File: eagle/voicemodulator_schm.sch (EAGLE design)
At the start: 38 parts, among them T1 2N5089, T2 2N5089, T3 2N5089, T4 2N5089

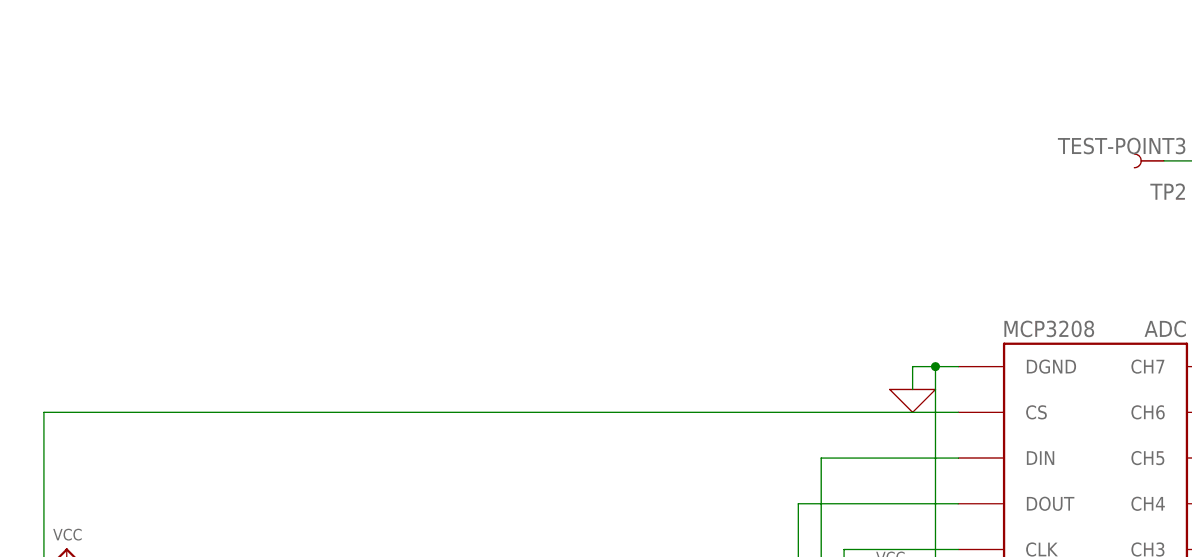
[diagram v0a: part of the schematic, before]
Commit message: USB 3.0 Type A Port Added, pinout TBD
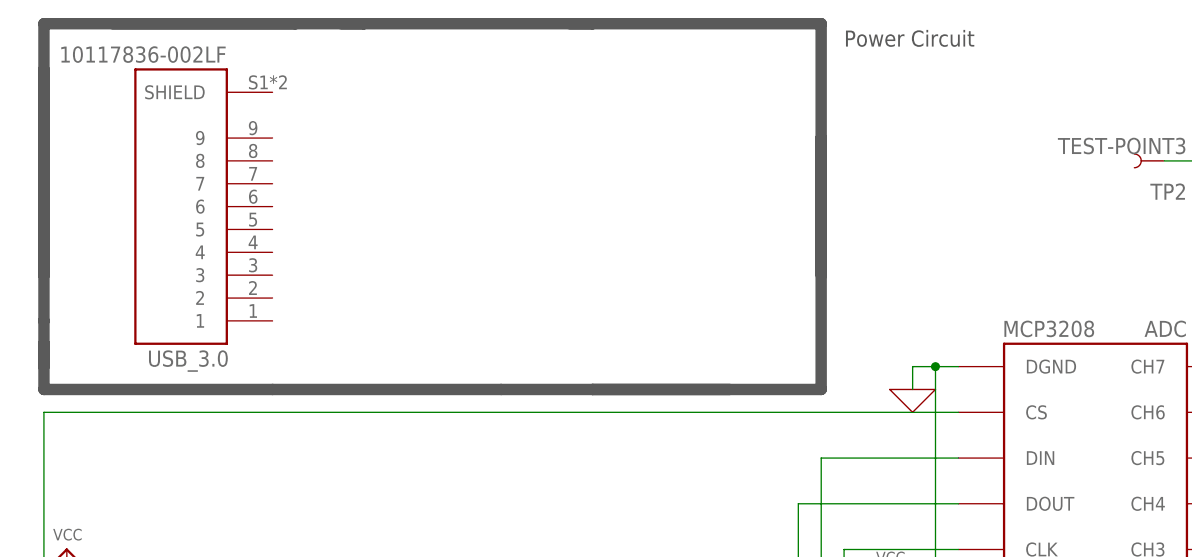
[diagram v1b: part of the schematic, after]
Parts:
- added USB_3.0: 10117836-002LF, USB_SMT_3:10117836-002LF
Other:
- note added: "Power Circuit"
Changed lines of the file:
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@@
 <part name="R18" library="resistor-shunt" library_urn="urn:adsk.eagle:library:346" deviceset="SMR-WAV" device="" package3d_urn="urn:adsk.eagle:package:25223/1"/>
 <part name="R19" library="resistor-shunt" library_urn="urn:adsk.eagle:library:346" deviceset="SMR-WAV" device="" package3d_urn="urn:adsk.eagle:package:25223/1"/>
+<part name="USB_3.0" library="USB_SMT_3" deviceset="10117836-002LF" device=""/>
 </parts>
 <sheets>
@@
 <wire x1="60.96" y1="-5.08" x2="60.96" y2="-33.02" width="1.27" layer="97"/>
 <text x="15.24" y="-2.54" size="1.778" layer="97">ISP Programming</text>
+<wire x1="-48.26" y1="83.82" x2="-48.26" y2="88.9" width="1.27" layer="97"/>
+<wire x1="-48.26" y1="88.9" x2="-48.26" y2="111.76" width="1.27" layer="97"/>
+<wire x1="-48.26" y1="88.9" x2="-48.26" y2="116.84" width="1.27" layer="97"/>
+<wire x1="38.1" y1="88.9" x2="38.1" y2="104.14" width="1.27" layer="97"/>
+<wire x1="38.1" y1="104.14" x2="38.1" y2="116.84" width="1.27" layer="97"/>
+<wire x1="38.1" y1="116.84" x2="12.7" y2="116.84" width="1.27" layer="97"/>
+<wire x1="12.7" y1="116.84" x2="10.16" y2="116.84" width="1.27" layer="97"/>
+<wire x1="12.7" y1="116.84" x2="-12.7" y2="116.84" width="1.27" layer="97"/>
+<wire x1="-12.7" y1="116.84" x2="-15.24" y2="116.84" width="1.27" layer="97"/>
+<wire x1="-12.7" y1="116.84" x2="-20.32" y2="116.84" width="1.27" layer="97"/>
+<wire x1="-20.32" y1="116.84" x2="-40.64" y2="116.84" width="1.27" layer="97"/>
+<wire x1="-20.32" y1="116.84" x2="-48.26" y2="116.84" width="1.27" layer="97"/>
+<wire x1="-48.26" y1="78.74" x2="-48.26" y2="81.28" width="1.27" layer="97"/>
+<wire x1="-48.26" y1="81.28" x2="-48.26" y2="83.82" width="1.27" layer="97"/>
+<wire x1="-22.86" y1="76.2" x2="-48.26" y2="76.2" width="1.27" layer="97"/>
+<wire x1="-48.26" y1="76.2" x2="-48.26" y2="81.28" width="1.27" layer="97"/>
+<wire x1="2.54" y1="76.2" x2="-22.86" y2="76.2" width="1.27" layer="97"/>
+<wire x1="27.94" y1="76.2" x2="12.7" y2="76.2" width="1.27" layer="97"/>
+<wire x1="12.7" y1="76.2" x2="2.54" y2="76.2" width="1.27" layer="97"/>
+<wire x1="38.1" y1="76.2" x2="12.7" y2="76.2" width="1.27" layer="97"/>
+<wire x1="38.1" y1="76.2" x2="38.1" y2="104.14" width="1.27" layer="97"/>
+<text x="40.64" y="114.3" size="1.778" layer="97">Power Circuit </text>
 </plain>
 <instances>
@@
 <attribute name="VALUE" x="130.81" y="48.641" size="1.778" layer="96" rot="R180"/>
 </instance>
+<instance part="USB_3.0" gate="G$1" x="-33.02" y="96.52" rot="R180">
+<attribute name="NAME" x="-27.686" y="80.518" size="1.778" layer="95" rot="R180"/>
+<attribute name="VALUE" x="-27.94" y="114.3" size="1.778" layer="96" rot="R180"/>
+</instance>
 </instances>

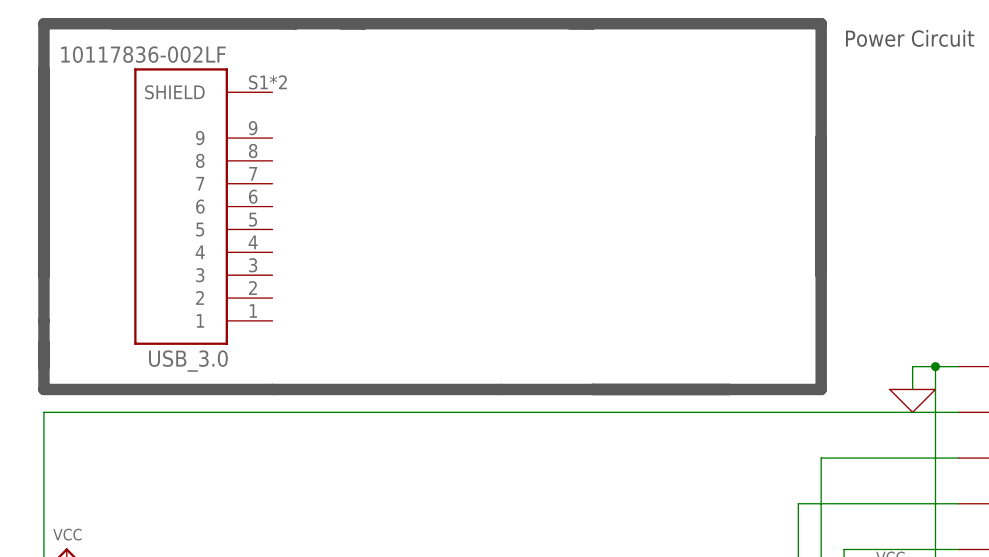
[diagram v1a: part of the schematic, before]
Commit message: Made USB 3.0 connections
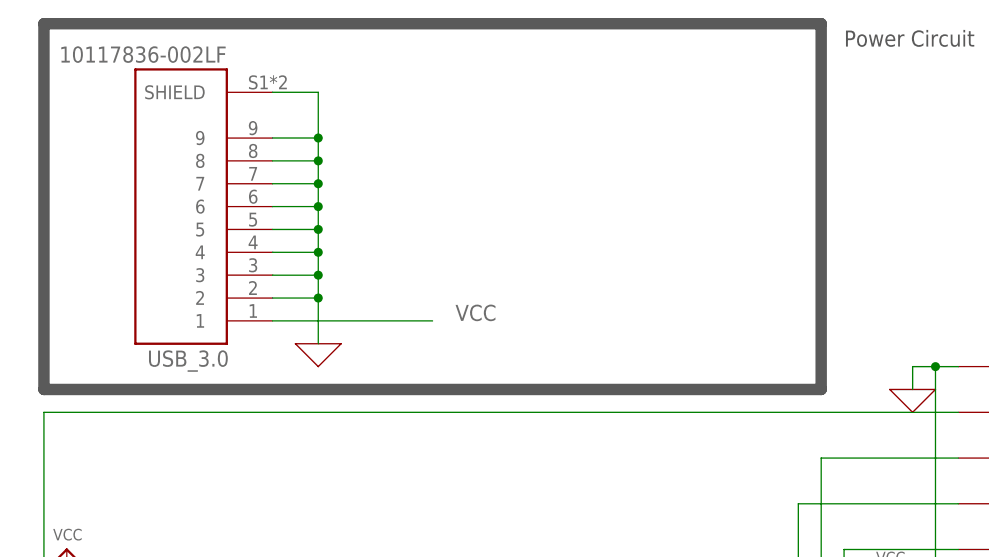
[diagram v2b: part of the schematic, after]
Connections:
- net 0: now also USB_3.0.2, USB_3.0.3, USB_3.0.4, USB_3.0.5, USB_3.0.6, USB_3.0.7, USB_3.0.8, USB_3.0.9, USB_3.0.SHIELD
- net VCC: now also USB_3.0.1
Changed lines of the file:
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@@
 <part name="R19" library="resistor-shunt" library_urn="urn:adsk.eagle:library:346" deviceset="SMR-WAV" device="" package3d_urn="urn:adsk.eagle:package:25223/1"/>
 <part name="USB_3.0" library="USB_SMT_3" deviceset="10117836-002LF" device=""/>
+<part name="X_11" library="ngspice-simulation" library_urn="urn:adsk.eagle:library:527439" deviceset="GND" device=""/>
 </parts>
 <sheets>
@@
 <wire x1="60.96" y1="-5.08" x2="60.96" y2="-33.02" width="1.27" layer="97"/>
 <text x="15.24" y="-2.54" size="1.778" layer="97">ISP Programming</text>
-<wire x1="-48.26" y1="83.82" x2="-48.26" y2="88.9" width="1.27" layer="97"/>
-<wire x1="-48.26" y1="88.9" x2="-48.26" y2="111.76" width="1.27" layer="97"/>
-<wire x1="-48.26" y1="88.9" x2="-48.26" y2="116.84" width="1.27" layer="97"/>
-<wire x1="38.1" y1="88.9" x2="38.1" y2="104.14" width="1.27" layer="97"/>
-<wire x1="38.1" y1="104.14" x2="38.1" y2="116.84" width="1.27" layer="97"/>
-<wire x1="38.1" y1="116.84" x2="12.7" y2="116.84" width="1.27" layer="97"/>
-<wire x1="12.7" y1="116.84" x2="10.16" y2="116.84" width="1.27" layer="97"/>
-<wire x1="12.7" y1="116.84" x2="-12.7" y2="116.84" width="1.27" layer="97"/>
-<wire x1="-12.7" y1="116.84" x2="-15.24" y2="116.84" width="1.27" layer="97"/>
-<wire x1="-12.7" y1="116.84" x2="-20.32" y2="116.84" width="1.27" layer="97"/>
-<wire x1="-20.32" y1="116.84" x2="-40.64" y2="116.84" width="1.27" layer="97"/>
-<wire x1="-20.32" y1="116.84" x2="-48.26" y2="116.84" width="1.27" layer="97"/>
-<wire x1="-48.26" y1="78.74" x2="-48.26" y2="81.28" width="1.27" layer="97"/>
-<wire x1="-48.26" y1="81.28" x2="-48.26" y2="83.82" width="1.27" layer="97"/>
-<wire x1="-22.86" y1="76.2" x2="-48.26" y2="76.2" width="1.27" layer="97"/>
-<wire x1="-48.26" y1="76.2" x2="-48.26" y2="81.28" width="1.27" layer="97"/>
-<wire x1="2.54" y1="76.2" x2="-22.86" y2="76.2" width="1.27" layer="97"/>
-<wire x1="27.94" y1="76.2" x2="12.7" y2="76.2" width="1.27" layer="97"/>
-<wire x1="12.7" y1="76.2" x2="2.54" y2="76.2" width="1.27" layer="97"/>
-<wire x1="38.1" y1="76.2" x2="12.7" y2="76.2" width="1.27" layer="97"/>
-<wire x1="38.1" y1="76.2" x2="38.1" y2="104.14" width="1.27" layer="97"/>
+<wire x1="-48.26" y1="76.2" x2="-48.26" y2="116.84" width="1.27" layer="97"/>
+<wire x1="38.1" y1="76.2" x2="38.1" y2="116.84" width="1.27" layer="97"/>
+<wire x1="38.1" y1="116.84" x2="-48.26" y2="116.84" width="1.27" layer="97"/>
+<wire x1="38.1" y1="76.2" x2="-48.26" y2="76.2" width="1.27" layer="97"/>
 <text x="40.64" y="114.3" size="1.778" layer="97">Power Circuit </text>
 </plain>
@@
 <attribute name="VALUE" x="-27.94" y="114.3" size="1.778" layer="96" rot="R180"/>
 </instance>
+<instance part="X_11" gate="G$1" x="-17.78" y="81.28"/>
 </instances>
 <busses>
@@
 <pinref part="X_3" gate="G$1" pin="0"/>
 <wire x1="167.64" y1="2.54" x2="167.64" y2="-7.62" width="0.1524" layer="91"/>
+</segment>
+<segment>
+<pinref part="USB_3.0" gate="G$1" pin="2"/>
+<pinref part="X_11" gate="G$1" pin="0"/>
+<wire x1="-22.86" y1="86.36" x2="-17.78" y2="86.36" width="0.1524" layer="91"/>
+<pinref part="USB_3.0" gate="G$1" pin="3"/>
+<wire x1="-17.78" y1="81.28" x2="-17.78" y2="86.36" width="0.1524" layer="91"/>
+<wire x1="-17.78" y1="86.36" x2="-17.78" y2="88.9" width="0.1524" layer="91"/>
+<wire x1="-17.78" y1="88.9" x2="-22.86" y2="88.9" width="0.1524" layer="91"/>
+<pinref part="USB_3.0" gate="G$1" pin="4"/>
+<wire x1="-22.86" y1="91.44" x2="-17.78" y2="91.44" width="0.1524" layer="91"/>
+<wire x1="-17.78" y1="91.44" x2="-17.78" y2="88.9" width="0.1524" layer="91"/>
+<junction x="-17.78" y="88.9"/>
+<junction x="-17.78" y="86.36"/>
+<pinref part="USB_3.0" gate="G$1" pin="7"/>
+<wire x1="-17.78" y1="91.44" x2="-17.78" y2="93.98" width="0.1524" layer="91"/>
+<wire x1="-17.78" y1="99.06" x2="-22.86" y2="99.06" width="0.1524" layer="91"/>
+<pinref part="USB_3.0" gate="G$1" pin="9"/>
+<wire x1="-22.86" y1="104.14" x2="-17.78" y2="104.14" width="0.1524" layer="91"/>
+<wire x1="-17.78" y1="104.14" x2="-17.78" y2="101.6" width="0.1524" layer="91"/>
+<pinref part="USB_3.0" gate="G$1" pin="6"/>
+<wire x1="-17.78" y1="101.6" x2="-17.78" y2="99.06" width="0.1524" layer="91"/>
+<wire x1="-17.78" y1="96.52" x2="-22.86" y2="96.52" width="0.1524" layer="91"/>
+<pinref part="USB_3.0" gate="G$1" pin="8"/>
+<wire x1="-22.86" y1="101.6" x2="-17.78" y2="101.6" width="0.1524" layer="91"/>
+<pinref part="USB_3.0" gate="G$1" pin="5"/>
+<wire x1="-17.78" y1="99.06" x2="-17.78" y2="96.52" width="0.1524" layer="91"/>
+<wire x1="-17.78" y1="96.52" x2="-17.78" y2="93.98" width="0.1524" layer="91"/>
+<wire x1="-17.78" y1="93.98" x2="-22.86" y2="93.98" width="0.1524" layer="91"/>
+<junction x="-17.78" y="101.6"/>
+<junction x="-17.78" y="99.06"/>
+<junction x="-17.78" y="96.52"/>
+<junction x="-17.78" y="93.98"/>
+<junction x="-17.78" y="91.44"/>
+<pinref part="USB_3.0" gate="G$1" pin="SHIELD"/>
+<wire x1="-22.86" y1="109.22" x2="-17.78" y2="109.22" width="0.1524" layer="91"/>
+<wire x1="-17.78" y1="109.22" x2="-17.78" y2="104.14" width="0.1524" layer="91"/>
+<junction x="-17.78" y="104.14"/>
 </segment>
 </net>
@@
 <wire x1="-45.72" y1="38.1" x2="-45.72" y2="55.88" width="0.1524" layer="91"/>
 </segment>
-</net>
+<segment>
+<pinref part="USB_3.0" gate="G$1" pin="1"/>
+<wire x1="-22.86" y1="83.82" x2="-5.08" y2="83.82" width="0.1524" layer="91"/>
+<label x="-2.54" y="83.82" size="1.778" layer="95"/>
+</segment>
+</net>

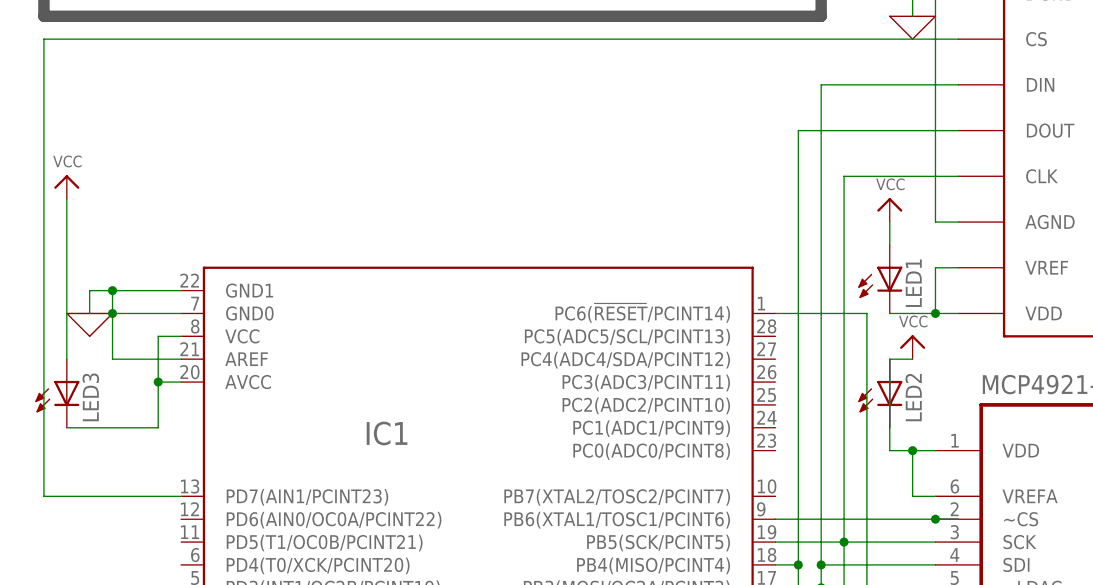
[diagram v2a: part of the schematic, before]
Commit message: Added name of LEDs and labeling for group/project on silk screen layer
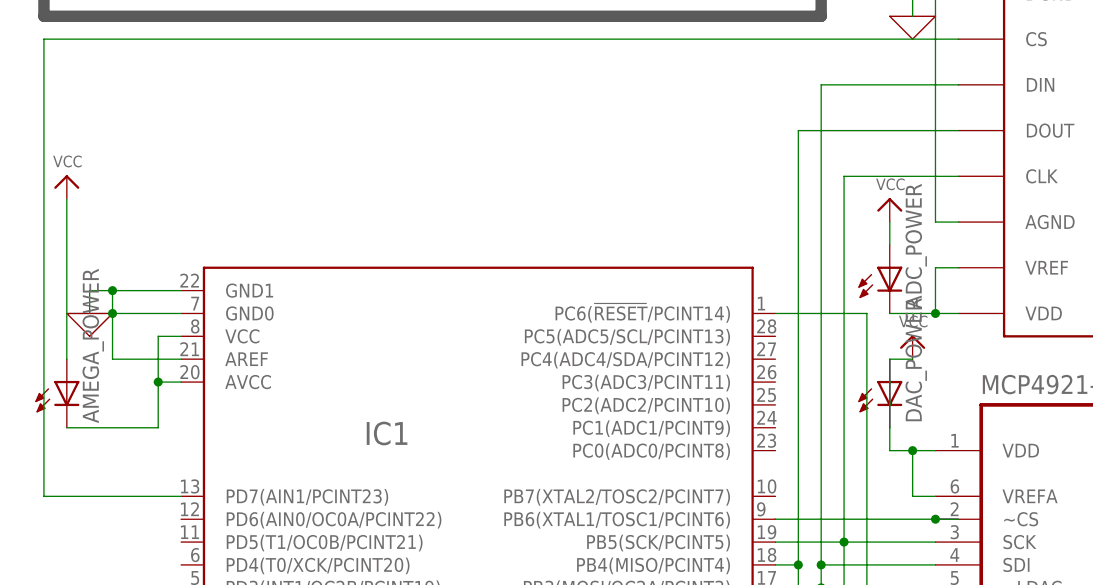
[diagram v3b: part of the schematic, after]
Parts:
- renumbered LED1 to ADC_POWER, LED2 to DAC_POWER, LED3 to AMEGA_POWER
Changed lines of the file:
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@@
 <part name="P+3" library="supply1" library_urn="urn:adsk.eagle:library:371" deviceset="VCC" device=""/>
 <part name="R15" library="resistor-shunt" library_urn="urn:adsk.eagle:library:346" deviceset="SMR-WAV" device="" package3d_urn="urn:adsk.eagle:package:25223/1"/>
-<part name="LED1" library="led" library_urn="urn:adsk.eagle:library:259" deviceset="LED" device="10MM" package3d_urn="urn:adsk.eagle:package:15828/1"/>
-<part name="LED2" library="led" library_urn="urn:adsk.eagle:library:259" deviceset="LED" device="10MM" package3d_urn="urn:adsk.eagle:package:15828/1"/>
-<part name="LED3" library="led" library_urn="urn:adsk.eagle:library:259" deviceset="LED" device="10MM" package3d_urn="urn:adsk.eagle:package:15828/1"/>
+<part name="ADC_POWER" library="led" library_urn="urn:adsk.eagle:library:259" deviceset="LED" device="10MM" package3d_urn="urn:adsk.eagle:package:15828/1"/>
+<part name="DAC_POWER" library="led" library_urn="urn:adsk.eagle:library:259" deviceset="LED" device="10MM" package3d_urn="urn:adsk.eagle:package:15828/1"/>
+<part name="AMEGA_POWER" library="led" library_urn="urn:adsk.eagle:library:259" deviceset="LED" device="10MM" package3d_urn="urn:adsk.eagle:package:15828/1"/>
 <part name="MIC_JACK1" library="SJ1-3523N" deviceset="SJ1-3523N" device=""/>
 <part name="X_3" library="ngspice-simulation" library_urn="urn:adsk.eagle:library:527439" deviceset="GND" device=""/>
@@
 <attribute name="VALUE" x="1.27" y="-10.541" size="1.778" layer="96"/>
 </instance>
-<instance part="LED1" gate="G$1" x="45.72" y="48.26">
+<instance part="ADC_POWER" gate="G$1" x="45.72" y="48.26">
 <attribute name="NAME" x="49.276" y="43.688" size="1.778" layer="95" rot="R90"/>
 <attribute name="VALUE" x="51.435" y="43.688" size="1.778" layer="96" rot="R90"/>
 </instance>
-<instance part="LED2" gate="G$1" x="45.72" y="35.56">
+<instance part="DAC_POWER" gate="G$1" x="45.72" y="35.56">
 <attribute name="NAME" x="49.276" y="30.988" size="1.778" layer="95" rot="R90"/>
 <attribute name="VALUE" x="51.435" y="30.988" size="1.778" layer="96" rot="R90"/>
 </instance>
-<instance part="LED3" gate="G$1" x="-45.72" y="35.56">
+<instance part="AMEGA_POWER" gate="G$1" x="-45.72" y="35.56">
 <attribute name="NAME" x="-42.164" y="30.988" size="1.778" layer="95" rot="R90"/>
 <attribute name="VALUE" x="-40.005" y="30.988" size="1.778" layer="96" rot="R90"/>
@@
 </segment>
 <segment>
-<pinref part="LED1" gate="G$1" pin="A"/>
+<pinref part="ADC_POWER" gate="G$1" pin="A"/>
 <pinref part="P+2" gate="VCC" pin="VCC"/>
 <wire x1="45.72" y1="50.8" x2="45.72" y2="53.34" width="0.1524" layer="91"/>
@@
 <segment>
 <pinref part="P+1" gate="VCC" pin="VCC"/>
-<pinref part="LED2" gate="G$1" pin="A"/>
+<pinref part="DAC_POWER" gate="G$1" pin="A"/>
 <wire x1="48.26" y1="38.1" x2="45.72" y2="38.1" width="0.1524" layer="91"/>
-<pinref part="LED2" gate="G$1" pin="C"/>
+<pinref part="DAC_POWER" gate="G$1" pin="C"/>
 <wire x1="45.72" y1="38.1" x2="45.72" y2="30.48" width="0.1524" layer="91"/>
 <pinref part="DAC" gate="A" pin="VDD"/>
@@
 </segment>
 <segment>
-<pinref part="LED3" gate="G$1" pin="A"/>
+<pinref part="AMEGA_POWER" gate="G$1" pin="A"/>
 <pinref part="P+5" gate="VCC" pin="VCC"/>
 <wire x1="-45.72" y1="38.1" x2="-45.72" y2="55.88" width="0.1524" layer="91"/>
@@
 <wire x1="48.26" y1="43.18" x2="50.8" y2="43.18" width="0.127" layer="91"/>
 <junction x="50.8" y="43.18"/>
-<pinref part="LED1" gate="G$1" pin="C"/>
+<pinref part="ADC_POWER" gate="G$1" pin="C"/>
 <wire x1="45.72" y1="43.18" x2="48.26" y2="43.18" width="0.1524" layer="91"/>
 </segment>
@@
 <wire x1="-33.02" y1="35.56" x2="-35.56" y2="35.56" width="0.1524" layer="91"/>
 <junction x="-35.56" y="35.56"/>
-<pinref part="LED3" gate="G$1" pin="C"/>
+<pinref part="AMEGA_POWER" gate="G$1" pin="C"/>
 <wire x1="-45.72" y1="30.48" x2="-35.56" y2="30.48" width="0.1524" layer="91"/>
 <wire x1="-35.56" y1="30.48" x2="-35.56" y2="35.56" width="0.1524" layer="91"/>
